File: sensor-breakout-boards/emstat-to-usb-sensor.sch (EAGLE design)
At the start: 4 parts, among them X1 Type-A Receptacle, X2 Micro Type-B Receptacle

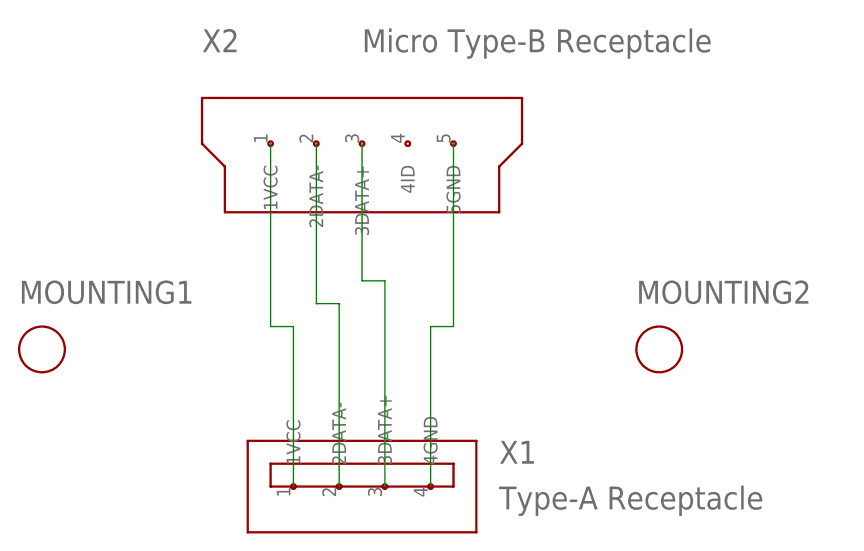
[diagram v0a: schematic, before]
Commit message: three breakout boards complete
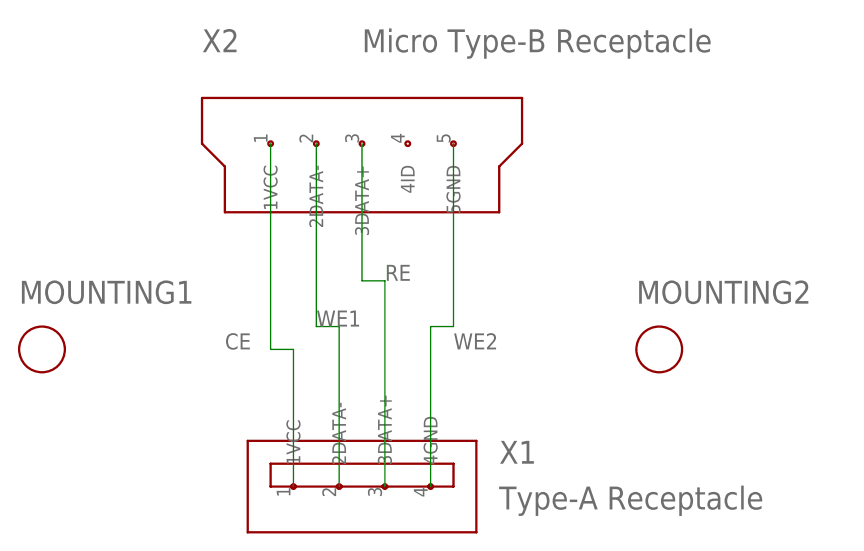
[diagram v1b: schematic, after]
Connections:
- net N$1 renamed CE
- net N$2 renamed WE1
- net N$3 renamed RE
- net N$4 renamed WE2
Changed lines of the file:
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@@
 </busses>
 <nets>
-<net name="N$1" class="0">
+<net name="CE" class="0">
 <segment>
 <pinref part="X1" gate="G$1" pin="1VCC"/>
-<wire x1="35.56" y1="17.78" x2="35.56" y2="35.56" width="0.1524" layer="91"/>
-<wire x1="35.56" y1="35.56" x2="33.02" y2="35.56" width="0.1524" layer="91"/>
+<wire x1="35.56" y1="17.78" x2="35.56" y2="33.02" width="0.1524" layer="91"/>
+<wire x1="35.56" y1="33.02" x2="33.02" y2="33.02" width="0.1524" layer="91"/>
 <pinref part="X2" gate="G$1" pin="1VCC"/>
-<wire x1="33.02" y1="35.56" x2="33.02" y2="55.88" width="0.1524" layer="91"/>
+<wire x1="33.02" y1="33.02" x2="33.02" y2="55.88" width="0.1524" layer="91"/>
+<label x="27.94" y="33.02" size="1.778" layer="95"/>
 </segment>
 </net>
-<net name="N$2" class="0">
+<net name="WE1" class="0">
 <segment>
 <pinref part="X2" gate="G$1" pin="2DATA-"/>
-<wire x1="38.1" y1="55.88" x2="38.1" y2="38.1" width="0.1524" layer="91"/>
+<wire x1="38.1" y1="55.88" x2="38.1" y2="35.56" width="0.1524" layer="91"/>
 <pinref part="X1" gate="G$1" pin="2DATA-"/>
-<wire x1="38.1" y1="38.1" x2="40.64" y2="38.1" width="0.1524" layer="91"/>
-<wire x1="40.64" y1="38.1" x2="40.64" y2="17.78" width="0.1524" layer="91"/>
+<wire x1="38.1" y1="35.56" x2="40.64" y2="35.56" width="0.1524" layer="91"/>
+<wire x1="40.64" y1="35.56" x2="40.64" y2="17.78" width="0.1524" layer="91"/>
+<label x="38.1" y="35.56" size="1.778" layer="95"/>
 </segment>
 </net>
-<net name="N$3" class="0">
+<net name="RE" class="0">
 <segment>
 <pinref part="X2" gate="G$1" pin="3DATA+"/>
@@
 <wire x1="43.18" y1="40.64" x2="45.72" y2="40.64" width="0.1524" layer="91"/>
 <wire x1="45.72" y1="40.64" x2="45.72" y2="17.78" width="0.1524" layer="91"/>
+<label x="45.72" y="40.64" size="1.778" layer="95"/>
 </segment>
 </net>
-<net name="N$4" class="0">
+<net name="WE2" class="0">
 <segment>
 <pinref part="X2" gate="G$1" pin="5GND"/>
@@
 <wire x1="53.34" y1="35.56" x2="50.8" y2="35.56" width="0.1524" layer="91"/>
 <wire x1="50.8" y1="35.56" x2="50.8" y2="17.78" width="0.1524" layer="91"/>
+<label x="53.34" y="33.02" size="1.778" layer="95"/>
 </segment>
 </net>

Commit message: made changes discussed at meeting
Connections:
- net WE1: now also X1.4GND, X2.5GND; no longer X1.2DATA-, X2.2DATA-
- net WE2: now also X1.2DATA-, X2.2DATA-; no longer X1.4GND, X2.5GND
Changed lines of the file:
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@@
 </segment>
 </net>
-<net name="WE1" class="0">
+<net name="WE2" class="0">
 <segment>
 <pinref part="X2" gate="G$1" pin="2DATA-"/>
@@
 </segment>
 </net>
-<net name="WE2" class="0">
+<net name="WE1" class="0">
 <segment>
 <pinref part="X2" gate="G$1" pin="5GND"/>
